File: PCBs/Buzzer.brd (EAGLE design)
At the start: 14.5 x 42 mm, 3 parts

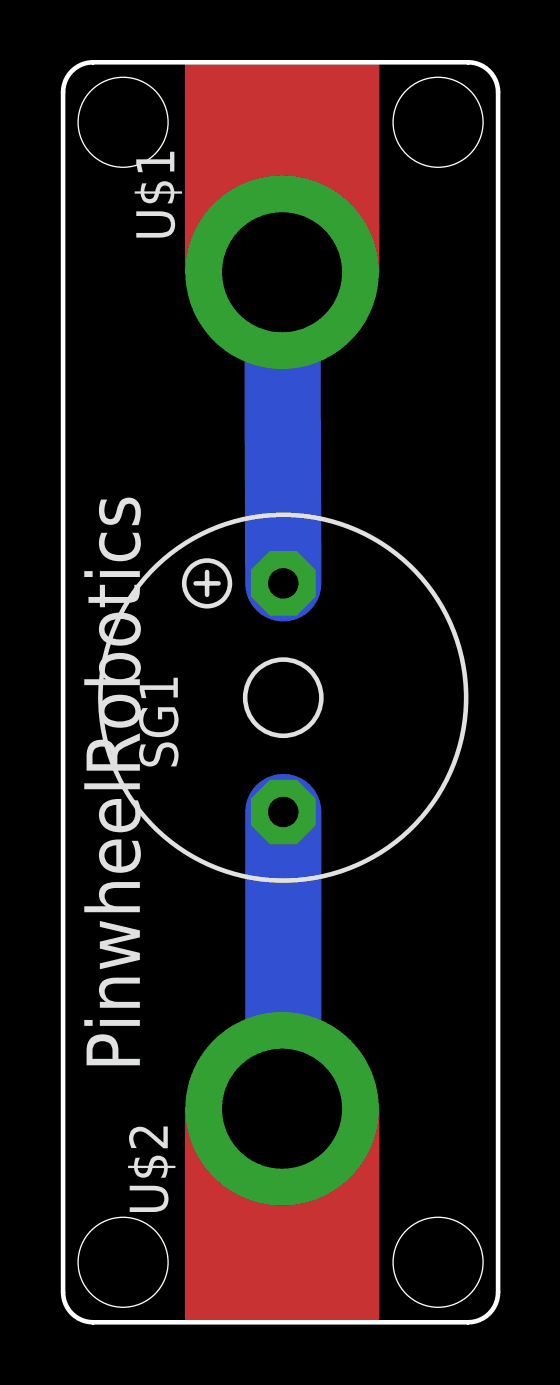
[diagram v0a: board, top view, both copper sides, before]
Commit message: Update for Dim width is 42 length is 28 for type 2 pcb
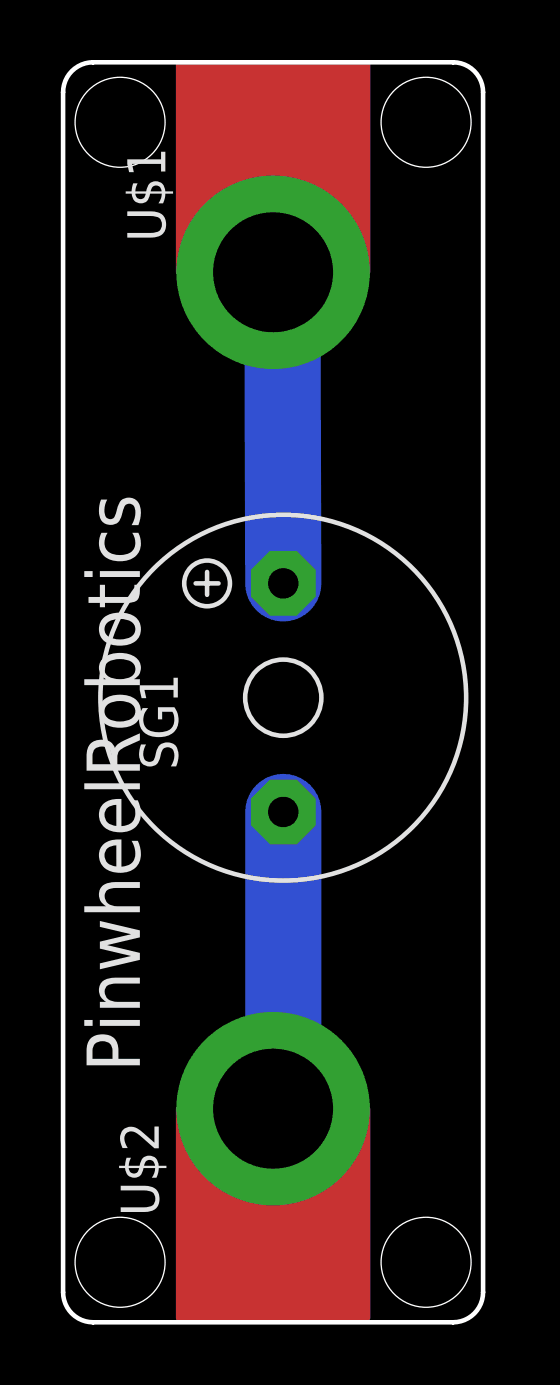
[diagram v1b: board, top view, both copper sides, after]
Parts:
- moved U$1 0.30 mm to (7.00, 35.0)
- moved U$2 0.30 mm to (7.00, 7.12)
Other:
- board size 14.5 x 42 mm -> 14 x 42 mm
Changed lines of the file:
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@@
 <drawing>
 <settings>
-<setting alwaysvectorfont="no"/>
+<setting alwaysvectorfont="yes"/>
 <setting verticaltext="up"/>
 </settings>
@@
 <board>
 <plain>
-<hole x="2" y="40" drill="3"/>
-<hole x="12.5" y="40" drill="3"/>
-<hole x="2" y="2" drill="3"/>
-<hole x="12.5" y="2" drill="3"/>
+<hole x="1.9" y="40" drill="3"/>
+<hole x="12.1" y="40" drill="3"/>
+<hole x="1.9" y="2" drill="3"/>
+<hole x="12.1" y="2" drill="3"/>
 <text x="13.54" y="26.05" size="1.778" layer="22" rot="MR270">care@pinwheel</text>
 <text x="2.56" y="8.35" size="1.778" layer="21" rot="R90">PinwheelRobotics</text>
-<wire x1="1" y1="0" x2="13.5" y2="0" width="0.1524" layer="20"/>
-<wire x1="13.5" y1="0" x2="14.5" y2="1" width="0.1524" layer="20" curve="90"/>
-<wire x1="14.5" y1="1" x2="14.5" y2="41" width="0.1524" layer="20"/>
-<wire x1="14.5" y1="41" x2="13.5" y2="42" width="0.1524" layer="20" curve="90"/>
-<wire x1="13.5" y1="42" x2="1" y2="42" width="0.1524" layer="20"/>
-<wire x1="1" y1="42" x2="0" y2="41" width="0.1524" layer="20" curve="90"/>
 <wire x1="0" y1="41" x2="0" y2="1" width="0.1524" layer="20"/>
 <wire x1="0" y1="1" x2="1" y2="0" width="0.1524" layer="20" curve="90"/>
+<wire x1="1" y1="0" x2="13" y2="0" width="0.1524" layer="20"/>
+<wire x1="13" y1="0" x2="14" y2="1" width="0.1524" layer="20" curve="90"/>
+<wire x1="14" y1="1" x2="14" y2="41" width="0.1524" layer="20"/>
+<wire x1="14" y1="41" x2="13" y2="42" width="0.1524" layer="20" curve="90"/>
+<wire x1="13" y1="42" x2="1" y2="42" width="0.1524" layer="20"/>
+<wire x1="1" y1="42" x2="0" y2="41" width="0.1524" layer="20" curve="90"/>
 <dimension x1="-2.5" y1="0" x2="-2.5" y2="42" x3="-5" y3="21" textsize="1.778" layer="1"/>
 <dimension x1="0" y1="43" x2="14.5" y2="43" x3="7.25" y3="47.5" textsize="1.778" layer="1"/>
+<dimension x1="0" y1="43" x2="14" y2="43" x3="7" y3="44.5" textsize="1.778" layer="1"/>
+<dimension x1="16.5" y1="2" x2="16.5" y2="40" x3="15.5" y3="21" textsize="1.778" layer="1"/>
 </plain>
 <attributes>
@@
 <attribute name="VALUE" x="11.15" y="17.01" size="1.27" layer="27" ratio="10" rot="R90"/>
 </element>
-<element name="U$1" library="microbit" package="MICROBIT_PAD" value="MICROBIT_PAD" x="7.3" y="35" smashed="yes" rot="R180">
-<attribute name="NAME" x="3.71" y="36.02" size="1.27" layer="21" rot="R90"/>
+<element name="U$1" library="microbit" package="MICROBIT_PAD" value="MICROBIT_PAD" x="7" y="35" smashed="yes" rot="R180">
+<attribute name="NAME" x="3.41" y="36.02" size="1.27" layer="21" rot="R90"/>
 </element>
-<element name="U$2" library="microbit" package="MICROBIT_PAD" value="MICROBIT_PAD" x="7.3" y="7.12" smashed="yes">
-<attribute name="NAME" x="3.49" y="3.54" size="1.27" layer="21" rot="R90"/>
+<element name="U$2" library="microbit" package="MICROBIT_PAD" value="MICROBIT_PAD" x="7" y="7.12" smashed="yes">
+<attribute name="NAME" x="3.19" y="3.54" size="1.27" layer="21" rot="R90"/>
 </element>
 </elements>
@@
 <contactref element="U$1" pad="PAD"/>
 <wire x1="7.34" y1="24.63" x2="7.30779375" y2="34.99220625" width="2.54" layer="16"/>
-<wire x1="7.30779375" y1="34.99220625" x2="7.3" y2="35" width="2.54" layer="16"/>
+<wire x1="7.30779375" y1="34.99220625" x2="7" y2="35" width="2.54" layer="16"/>
 </signal>
 <signal name="N$2">
@@
 <wire x1="7.34" y1="17.01" x2="7.34" y2="7.36" width="2.54" layer="16"/>
 <wire x1="7.34" y1="7.36" x2="7.8" y2="6.9" width="2.54" layer="16"/>
-<wire x1="7.8" y1="6.9" x2="7.3" y2="7.12" width="0" layer="19" extent="16-16"/>
+<wire x1="7.8" y1="6.9" x2="7" y2="7.12" width="0" layer="19" extent="16-16"/>
 <wire x1="6.917034375" y1="4.382634375" x2="7.8" y2="6.9" width="0" layer="19" extent="16-16"/>
 </signal>

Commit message: Corrected hole position for some design , made transistor as switch as category 1
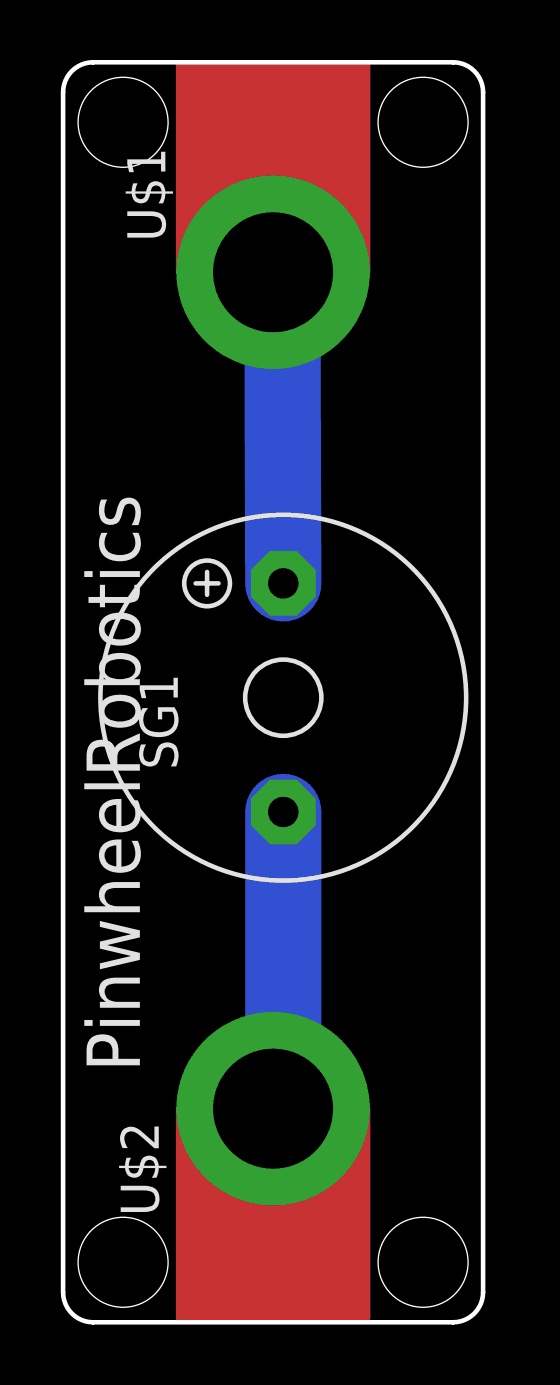
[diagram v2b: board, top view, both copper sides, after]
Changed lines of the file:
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@@
 <drawing>
 <settings>
-<setting alwaysvectorfont="yes"/>
+<setting alwaysvectorfont="no"/>
 <setting verticaltext="up"/>
 </settings>
@@
 <board>
 <plain>
-<hole x="1.9" y="40" drill="3"/>
-<hole x="12.1" y="40" drill="3"/>
-<hole x="1.9" y="2" drill="3"/>
-<hole x="12.1" y="2" drill="3"/>
+<hole x="2" y="40" drill="3"/>
+<hole x="12" y="40" drill="3"/>
+<hole x="2" y="2" drill="3"/>
+<hole x="12" y="2" drill="3"/>
 <text x="13.54" y="26.05" size="1.778" layer="22" rot="MR270">care@pinwheel</text>
 <text x="2.56" y="8.35" size="1.778" layer="21" rot="R90">PinwheelRobotics</text>
